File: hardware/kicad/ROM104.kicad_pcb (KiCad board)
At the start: 2 copper layers, 100 x 85 mm, 46 parts, among them J1 Screw_Terminal_01x06, J2 Screw_Terminal_01x06, J3 CAN, J4 Screw_Terminal_01x06, K1 SPDT_RELAY, K2 SPDT_RELAY, K3 SPDT_RELAY, K4 SPDT_RELAY, K5 SPDT_RELAY, K6 SPDT_RELAY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

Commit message: Tweaks
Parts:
- removed RN1: R_Network08, Resistor_THT:R_Array_SIP9
- added D9: LED, LED_THT:LED_D1.8mm_W3.3mm_H2.4mm, F.Cu at (221.9, 115.2)
- added R10: 470R, Resistor_THT:R_Axial_DIN0207_L6.3mm_D2.5mm_P2.54mm_Vertical, F.Cu at (215.3, 117.9)
- added R11: 470R, Resistor_THT:R_Axial_DIN0207_L6.3mm_D2.5mm_P2.54mm_Vertical, F.Cu at (218.6, 117.9)
- added R3: 470R, Resistor_THT:R_Axial_DIN0207_L6.3mm_D2.5mm_P2.54mm_Vertical, F.Cu at (221.9, 117.9)
- added R4: 470R, Resistor_THT:R_Axial_DIN0207_L6.3mm_D2.5mm_P2.54mm_Vertical, F.Cu at (195.5, 117.9)
- added R5: 470R, Resistor_THT:R_Axial_DIN0207_L6.3mm_D2.5mm_P2.54mm_Vertical, F.Cu at (198.8, 117.9)
- added R6: 470R, Resistor_THT:R_Axial_DIN0207_L6.3mm_D2.5mm_P2.54mm_Vertical, F.Cu at (202.1, 117.9)
- added R7: 470R, Resistor_THT:R_Axial_DIN0207_L6.3mm_D2.5mm_P2.54mm_Vertical, F.Cu at (205.4, 117.9)
- added R8: 470R, Resistor_THT:R_Axial_DIN0207_L6.3mm_D2.5mm_P2.54mm_Vertical, F.Cu at (208.7, 117.9)
- added R9: 470R, Resistor_THT:R_Axial_DIN0207_L6.3mm_D2.5mm_P2.54mm_Vertical, F.Cu at (212.0, 117.9)
- R1: footprint Resistor_THT:R_Axial_DIN0207_L6.3mm_D2.5mm_P7.62mm_Horizontal -> Resistor_THT:R_Axial_DIN0207_L6.3mm_D2.5mm_P2.54mm_Vertical
- moved R1 5.08 mm to (147.5, 102.7)
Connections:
- U7 pad 17: Net-(U7-Pad17) -> /TRANSMIT_LED
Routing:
- net /TRANSMIT_LED: track 0.00 -> 72.4 mm
- net Net-(D1-Pad1): track 6.60 -> 2.73 mm
- net +5V: track 526.3 -> 529.9 mm
- net Net-(D5-Pad1): track 5.83 -> 2.73 mm
- net Net-(D9-Pad1): track 0.00 -> 2.73 mm
- net Net-(D2-Pad1): track 5.83 -> 3.17 mm
- net Net-(D6-Pad1): track 4.31 -> 2.73 mm
- net Net-(D3-Pad1): track 3.99 -> 2.73 mm
- net Net-(D7-Pad1): track 3.68 -> 2.73 mm
- net Net-(D4-Pad1): track 3.36 -> 2.73 mm
- net GND: vias 40 -> 41

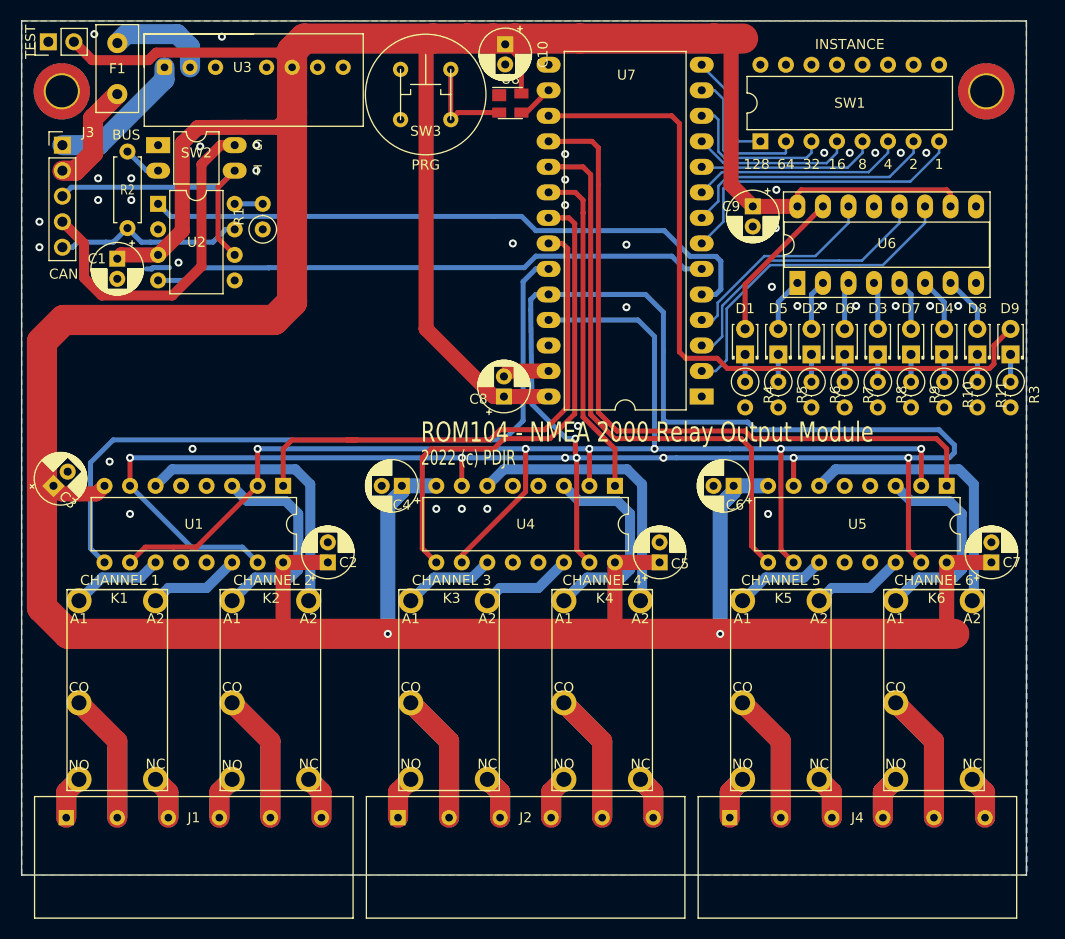
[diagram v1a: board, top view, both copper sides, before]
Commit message: PCB reroute
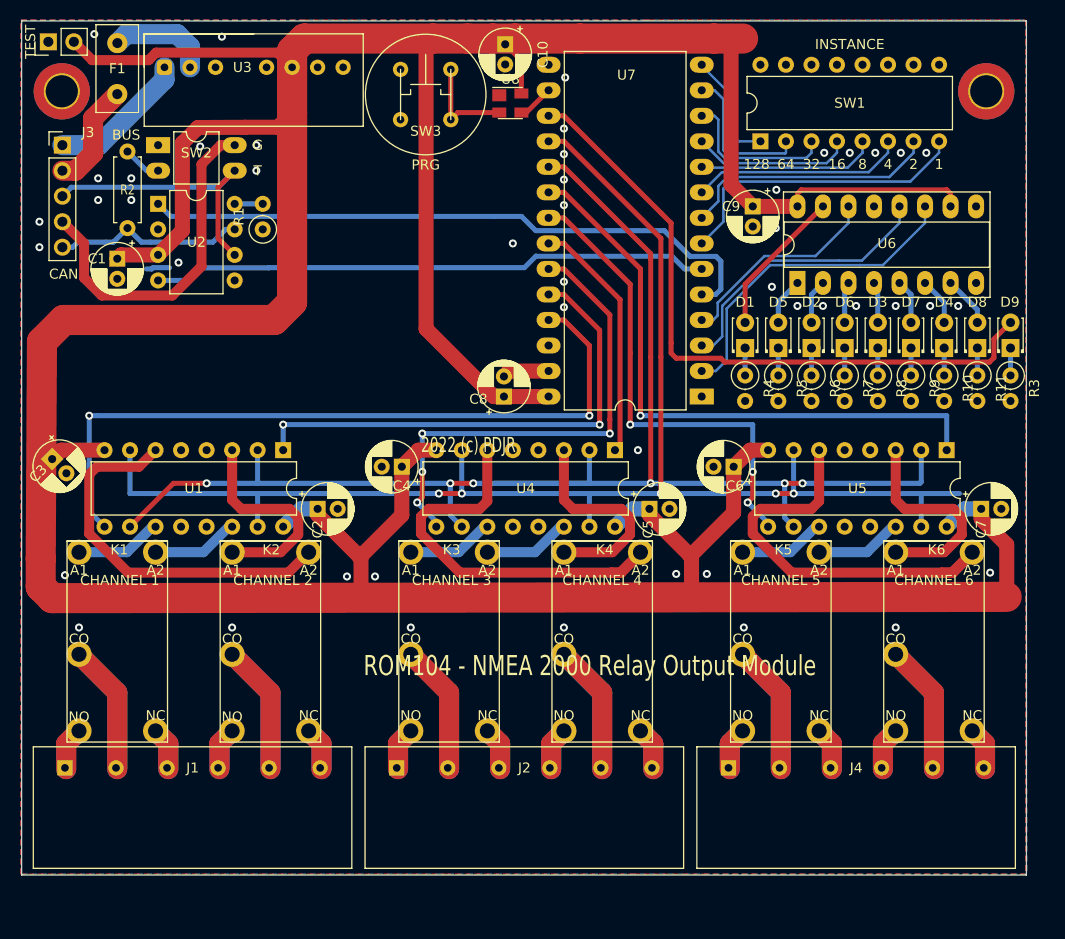
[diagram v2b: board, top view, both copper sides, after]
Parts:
- moved C2 5.43 mm to (153.0, 130.6), turned to 0 degrees
- moved C5 5.43 mm to (186.0, 130.6), turned to 0 degrees
- moved C7 5.43 mm to (219.0, 130.6), turned to 0 degrees
- moved J1 4.95 mm to (153.2, 156.3)
- moved J2 4.95 mm to (186.2, 156.3)
- moved J4 4.95 mm to (219.3, 156.3)
- moved K1 4.83 mm to (129.2, 152.7)
- moved K2 4.83 mm to (144.4, 152.7)
- moved K3 4.83 mm to (162.2, 152.7)
- moved K4 4.83 mm to (177.5, 152.7)
- moved K5 4.83 mm to (195.2, 152.7)
- moved K6 4.83 mm to (210.5, 152.7)
- moved U1 3.56 mm to (149.5, 124.7)
- moved U4 3.56 mm to (182.6, 124.7)
- moved U5 3.56 mm to (215.6, 124.7)
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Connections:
- U7 pad 18: /CH6_EN -> /SET
- U7 pad 19: /CH5_EN -> /RST
- U7 pad 20: /CH4_EN -> /CH6_EN
- U7 pad 21: /CH3_EN -> /CH5_EN
- U7 pad 22: /CH2_EN -> /CH4_EN
- U7 pad 23: /CH1_EN -> /CH3_EN
- U7 pad 24: /SET -> /CH2_EN
- U7 pad 25: /RST -> /CH1_EN
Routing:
- net +5V: track 529.9 -> 443.0 mm, vias 2 -> 0
- net /SET: track 202.1 -> 146.0 mm, vias 8 -> 5
- net Net-(K6-Pad2): track 28.4 -> 42.3 mm
- net Net-(K4-Pad2): track 28.4 -> 42.2 mm
- net /CH6_EN: track 71.4 -> 60.8 mm, vias 0 -> 1
- net /CH5_EN: track 57.8 -> 48.2 mm, vias 0 -> 3
- net Net-(K2-Pad2): track 28.4 -> 37.8 mm
- net /CH4_EN: track 33.5 -> 24.6 mm
- net /TRANSMIT_LED: track 72.4 -> 66.4 mm
- net /RST: track 141.2 -> 146.5 mm
- net /CH2_EN: track 52.6 -> 50.0 mm, vias 0 -> 2
- net /CH1_EN: track 72.2 -> 73.6 mm, vias 0 -> 2
- net /CH3_EN: track 49.7 -> 48.7 mm, vias 0 -> 4
- net Net-(D8-Pad2): track 5.68 -> 5.04 mm
- net Net-(D7-Pad2): track 5.05 -> 4.41 mm
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
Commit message: Refactor
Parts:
- K1, K2, K3, K4, K5, K6: value SPDT_RELAY -> PE014F05; footprint PDJR-connectors:PE014F05 -> PDJR_Relays:PE014F05
- U3: footprint PDJR-connectors:TMR_2411 -> PDJR_DC-DC_Converters:TMR_2411
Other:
- board text added: "ROM104 NMEA 2000 Relay Output Module"
- board text removed: "ROM104 - NMEA 2000 Relay Output Module"

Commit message: Refactor
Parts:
- J1, J2, J4: footprint PDJR-connectors:879-1272_TERMINAL_HEADER_6-POLE -> PDJR_Connectors:879-1272_TERMINAL_HEADER_6-POLE

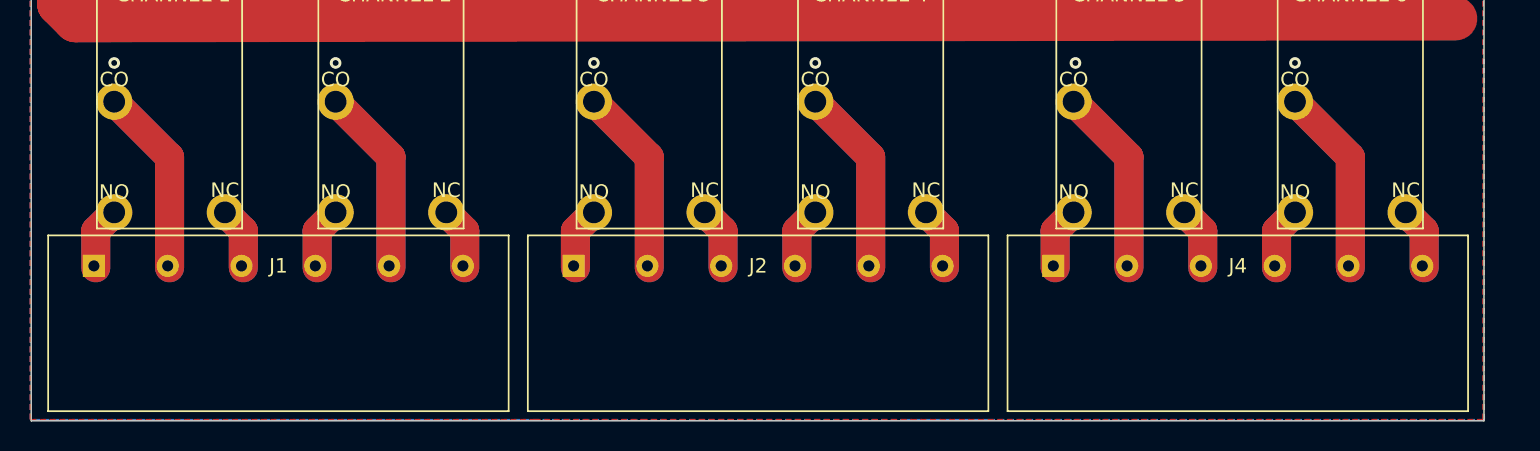
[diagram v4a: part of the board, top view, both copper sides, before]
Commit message: Change relay terminal
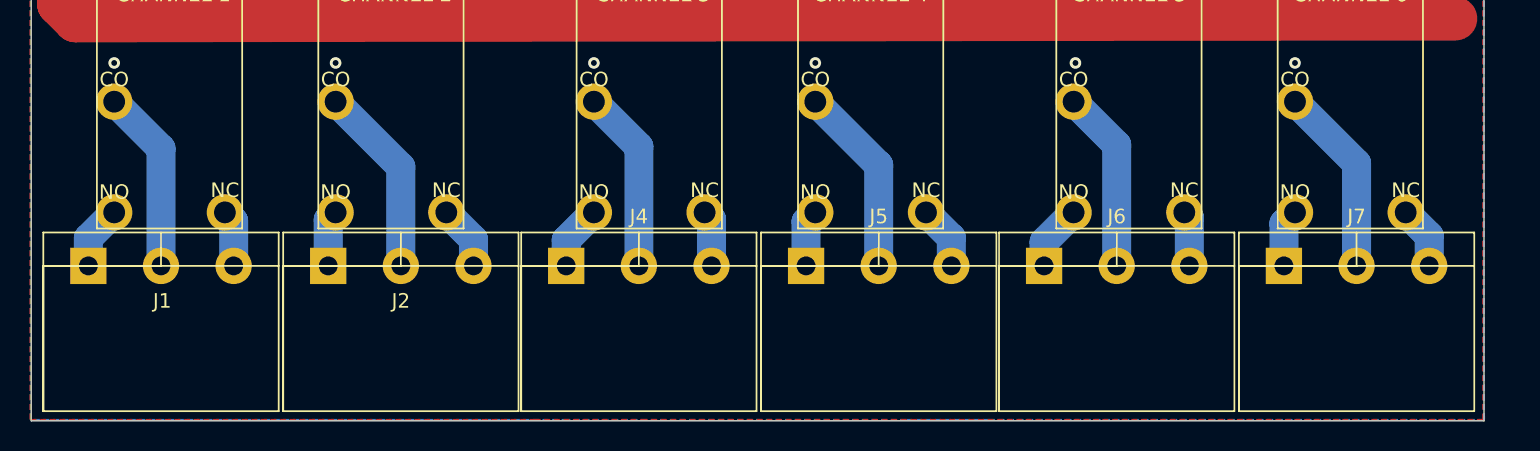
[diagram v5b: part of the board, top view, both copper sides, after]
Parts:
- added J5: Screw_Terminal_01x03, PDJR_Connectors:8971187_3_PIN_5MM_PLUGGABLE_HEADER, F.Cu at (176.8, 156.3)
- added J6: Screw_Terminal_01x03, PDJR_Connectors:8971187_3_PIN_5MM_PLUGGABLE_HEADER, F.Cu at (193.2, 156.3)
- added J7: Screw_Terminal_01x03, PDJR_Connectors:8971187_3_PIN_5MM_PLUGGABLE_HEADER, F.Cu at (209.7, 156.3)
- J1, J2, J4: value Screw_Terminal_01x06 -> Screw_Terminal_01x03; footprint PDJR_Connectors:879-1272_TERMINAL_HEADER_6-POLE -> PDJR_Connectors:8971187_3_PIN_5MM_PLUGGABLE_HEADER
- moved J4 58.9 mm to (160.3, 156.3), turned to 0 degrees
- moved J2 42.3 mm to (143.9, 156.3), turned to 0 degrees
- moved J1 25.8 mm to (127.4, 156.3), turned to 0 degrees
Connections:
- K2 pad 1: Net-(J1-Pad6) -> Net-(J2-Pad3)
- K2 pad 14: Net-(J1-Pad4) -> Net-(J2-Pad1)
- K2 pad 7: Net-(J1-Pad5) -> Net-(J2-Pad2)
- K3 pad 1: Net-(J2-Pad3) -> Net-(J4-Pad3)
- K3 pad 14: Net-(J2-Pad1) -> Net-(J4-Pad1)
- K3 pad 7: Net-(J2-Pad2) -> Net-(J4-Pad2)
- K4 pad 1: Net-(J2-Pad6) -> Net-(J5-Pad3)
- K4 pad 14: Net-(J2-Pad4) -> Net-(J5-Pad1)
- K4 pad 7: Net-(J2-Pad5) -> Net-(J5-Pad2)
- K5 pad 1: Net-(J4-Pad3) -> Net-(J6-Pad3)
- K5 pad 14: Net-(J4-Pad1) -> Net-(J6-Pad1)
- K5 pad 7: Net-(J4-Pad2) -> Net-(J6-Pad2)
- K6 pad 1: Net-(J4-Pad6) -> Net-(J7-Pad3)
- K6 pad 14: Net-(J4-Pad4) -> Net-(J7-Pad1)
- K6 pad 7: Net-(J4-Pad5) -> Net-(J7-Pad2)
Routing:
- net Net-(J4-Pad5): track 26.0 -> 0.00 mm
- net Net-(J2-Pad5): track 26.0 -> 0.00 mm
- net Net-(J1-Pad5): track 26.0 -> 0.00 mm
- net Net-(J4-Pad2): track 26.0 -> 12.6 mm
- net Net-(J1-Pad2): track 26.0 -> 12.6 mm
- net Net-(J5-Pad2): track 0.00 -> 13.1 mm
- net Net-(J7-Pad2): track 0.00 -> 13.1 mm
- net Net-(J2-Pad2): track 26.0 -> 13.2 mm
- net Net-(J6-Pad2): track 0.00 -> 12.5 mm
- net Net-(J4-Pad4): track 8.67 -> 0.00 mm
- net Net-(J2-Pad6): track 8.67 -> 0.00 mm
- net Net-(J2-Pad4): track 8.67 -> 0.00 mm
- net Net-(J1-Pad6): track 8.67 -> 0.00 mm
- net Net-(J4-Pad6): track 8.67 -> 0.00 mm
- net Net-(J1-Pad4): track 8.67 -> 0.00 mm
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
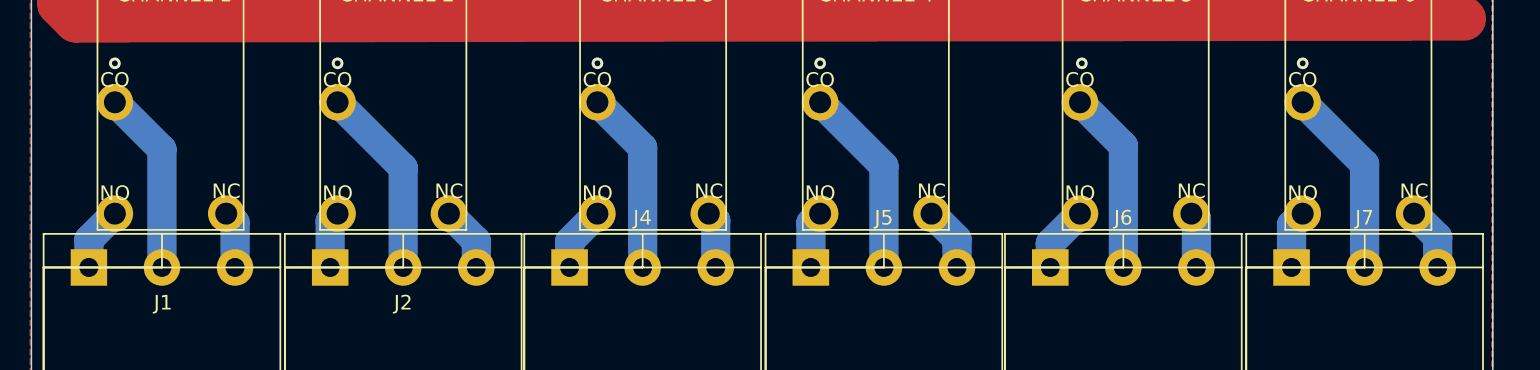
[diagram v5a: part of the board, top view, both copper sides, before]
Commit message: PCB reroute
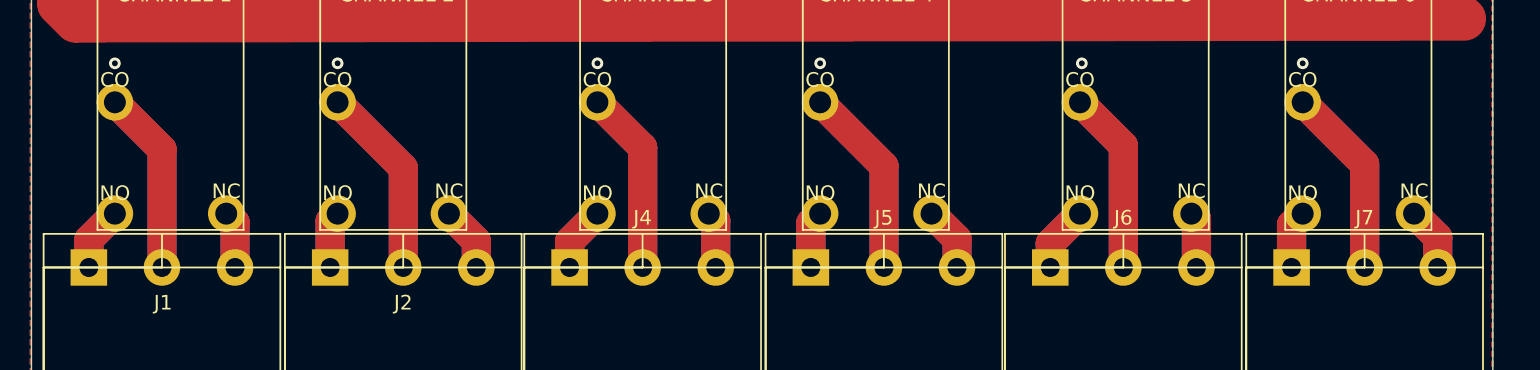
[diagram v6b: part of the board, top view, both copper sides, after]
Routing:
- net Net-(J2-Pad2): track 13.2 -> 26.3 mm
- net Net-(J5-Pad2): track 13.1 -> 26.2 mm
- net Net-(J7-Pad2): track 13.1 -> 26.1 mm
- net Net-(J1-Pad2): track 12.6 -> 25.3 mm
- net Net-(J4-Pad2): track 12.6 -> 25.2 mm
- net Net-(J6-Pad2): track 12.5 -> 25.1 mm
- net Net-(J6-Pad1): track 4.52 -> 9.05 mm
- net Net-(J4-Pad1): track 4.47 -> 8.94 mm
- net Net-(J2-Pad3): track 4.46 -> 8.92 mm
- net Net-(J1-Pad1): track 4.42 -> 8.84 mm
- net Net-(J5-Pad3): track 4.41 -> 8.81 mm
- net Net-(J7-Pad3): track 4.35 -> 8.71 mm
- net Net-(J7-Pad1): track 4.00 -> 8.00 mm
- net Net-(J5-Pad1): track 3.95 -> 7.89 mm
- net Net-(J1-Pad3): track 3.93 -> 7.86 mm
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
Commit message: Tweak
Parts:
- removed the REF** at (127.5, 89.0)
- removed the REF** at (219.5, 89.0)
- added REF**: MountingHole_3.2mm_M3_DIN965_Pad_TopBottom, MountingHole:MountingHole_3.2mm_M3_DIN965_Pad_TopBottom, F.Cu at (24.0, 27.0)
- added REF**: MountingHole_3.2mm_M3_DIN965_Pad_TopBottom, MountingHole:MountingHole_3.2mm_M3_DIN965_Pad_TopBottom, F.Cu at (116.0, 27.0)
- moved C1 120.6 mm to (29.5, 43.7)
- moved C5 120.6 mm to (82.5, 68.6)
- moved D5 120.6 mm to (95.3, 52.6)
- moved D7 120.6 mm to (108.5, 52.6)
- moved F1 120.6 mm to (29.5, 27.3)
- moved J5 120.6 mm to (73.3, 94.3)
- moved J7 120.6 mm to (106.2, 94.3)
- moved K6 120.6 mm to (107.0, 90.7)
- moved R5 120.6 mm to (95.3, 55.3)
- moved R9 120.6 mm to (108.5, 55.3)
- moved U4 120.6 mm to (79.0, 62.7)
- moved U6 120.6 mm to (97.2, 46.1)
- moved C2 120.6 mm to (49.5, 68.6)
- moved C3 120.6 mm to (23.0, 63.6)
- moved C4 120.6 mm to (57.8, 64.4)
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
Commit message: Tweak
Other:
- board text added: "CONNECT BUS SHIELD TO GROUND"
- board text added: "ROM104 20221101 (c) PDJR/Paul Reeve NMEA 2000 Relay Output Module"
- board text added: "TERMINATE BUS (120R)"
- board text removed: "2022 (c) PDJR"
- board text removed: "CHANNEL 1"
- board text removed: "CHANNEL 2"
- board text removed: "CHANNEL 3"
- board text removed: "CHANNEL 4"
- board text removed: "CHANNEL 5"
- board text removed: "CHANNEL 6"
- board text removed: "G"
- board text removed: "ROM104 NMEA 2000 Relay Output Module"
- board text removed: "T"
